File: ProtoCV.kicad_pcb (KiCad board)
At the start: 2 copper layers, 100 x 100 mm, 141 parts, among them J1 AudioJack2_SwitchT, J10 Conn_01x01_Male, J11 Conn_01x05_Male, J12 Conn_01x09_Male, J13 AudioJack2_SwitchT, J14 AudioJack2_SwitchT, J15 AudioJack2_SwitchT, J16 AudioJack2_SwitchT, J17 AudioJack2_SwitchT, J18 AudioJack2_SwitchT, J19 AudioJack2_SwitchT, J2 AudioJack2_SwitchT, J20 AudioJack2_SwitchT, J21 Conn_01x01_Male, J22 Conn_01x01_Male, J23 Conn_01x01_Male, J24 Conn_01x01_Male, J25 Conn_01x01_Male, J26 Conn_01x01_Male, J27 Conn_01x01_Male, J28 Conn_01x01_Male, J29 Conn_01x01_Male, J3 AudioJack2_SwitchT, J30 Conn_01x01_Male, J4 AudioJack2_SwitchT, J5 AudioJack2_SwitchT, J6 AudioJack2_SwitchT, J7 AudioJack2_SwitchT, J8 AudioJack2_SwitchT, J9 Conn_02x05_Odd_Even, Q1 BC847, Q2 BC847, Q3 BC847, Q4 BC847, Q5 BC847, Q6 BC847, Q7 BC847, Q8 BC847, U1 OPA4192, U2 OPA4192, U3 ADC80508Z, U4 R-78E3.3-0.5, U5 LD2981ABU33TR, U6 74AHCT244, U7 L7805

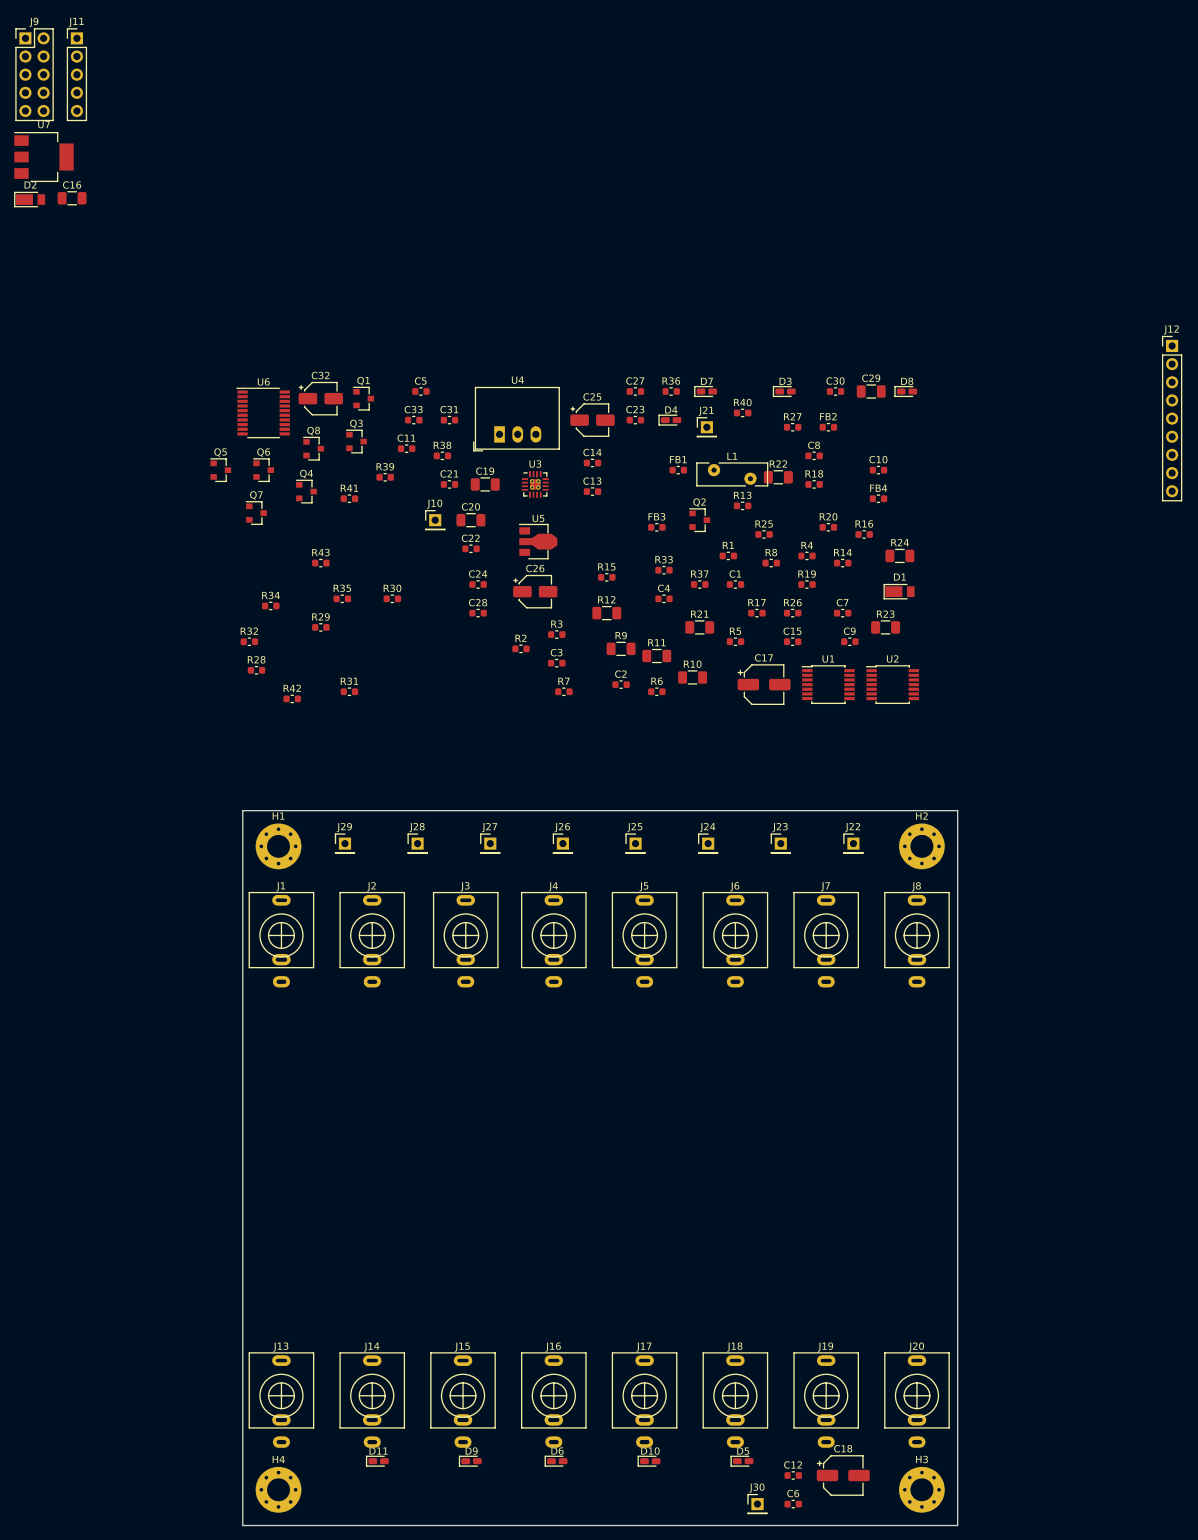
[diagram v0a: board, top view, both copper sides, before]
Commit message: Completed placement.
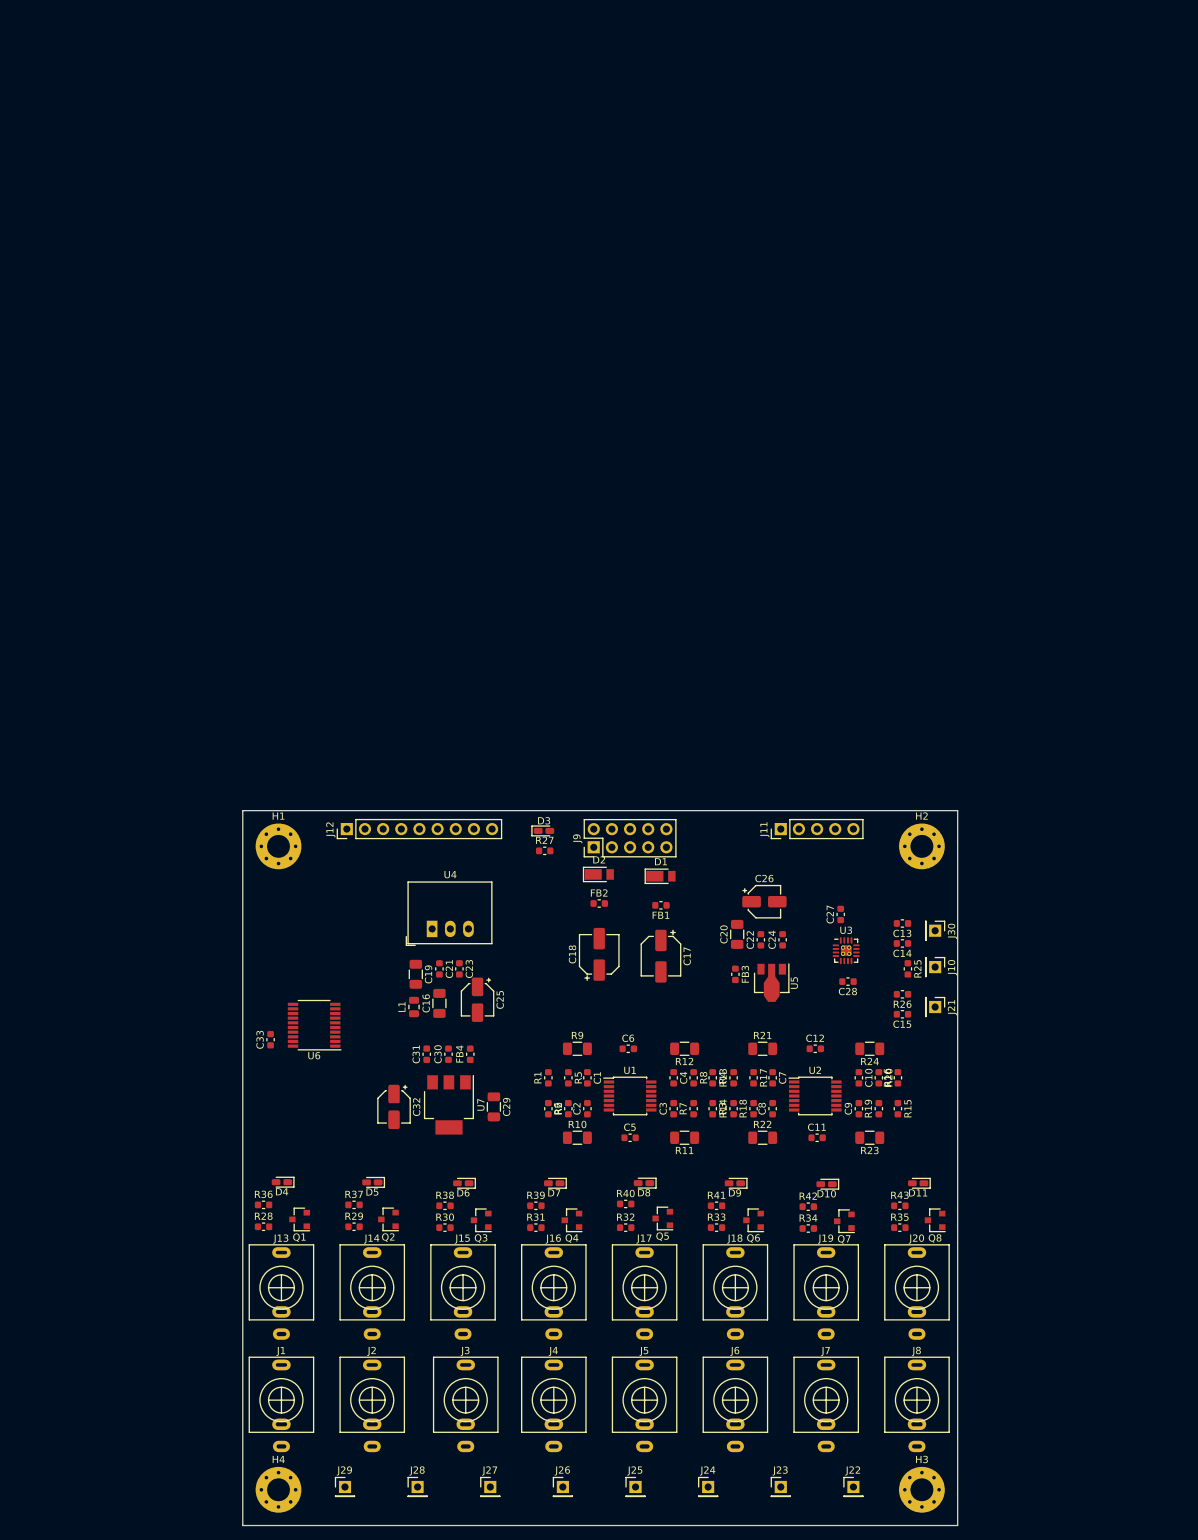
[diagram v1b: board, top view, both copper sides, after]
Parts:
- L1: footprint Fuse:Fuse_Bourns_MF-RHT100 -> Inductor_SMD:L_0805_2012Metric
- moved J11 148.1 mm to (175.3, 52.6), turned to 90 degrees
- moved U7 144.2 mm to (128.8, 91.2), turned to 270 degrees
- moved Q8 138.6 mm to (196.8, 107.3), turned to 180 degrees
- moved J9 138.3 mm to (149.1, 55.1), turned to 90 degrees
- moved J12 133.8 mm to (114.6, 52.6), turned to 90 degrees
- moved Q7 128.7 mm to (184.2, 107.4), turned to 180 degrees
- moved R36 127.3 mm to (102.9, 105.1)
- moved Q6 125.3 mm to (171.4, 107.3), turned to 180 degrees
- moved C16 123.8 mm to (127.5, 77.0), turned to 90 degrees
- moved D2 123.5 mm to (149.9, 58.9)
- moved Q5 121.6 mm to (158.8, 107.1), turned to 180 degrees
- moved R43 121.0 mm to (191.9, 105.3)
- moved D4 119.7 mm to (105.5, 102.0), turned to 180 degrees
- moved R35 117.6 mm to (191.9, 108.3)
- moved D8 116.7 mm to (156.1, 102.1), turned to 180 degrees
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
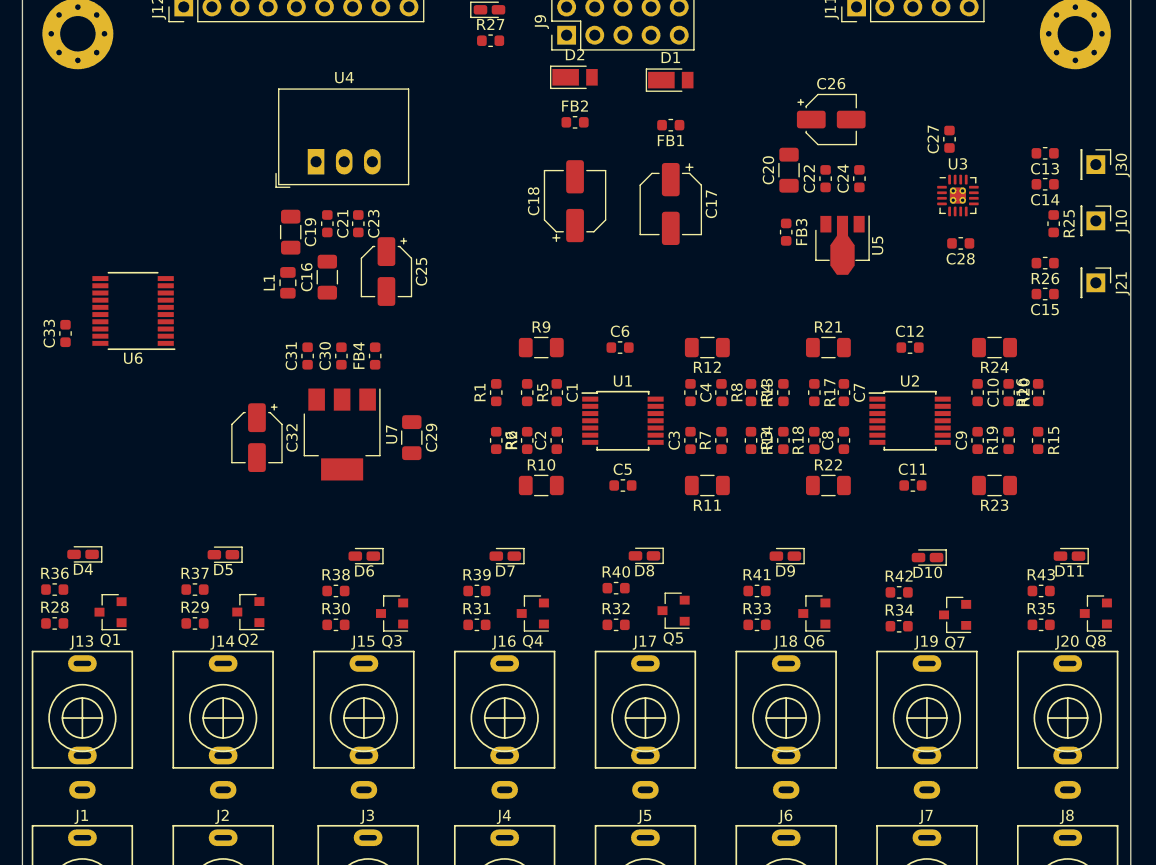
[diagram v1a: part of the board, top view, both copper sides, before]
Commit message: Improved placement with separate analogue section.
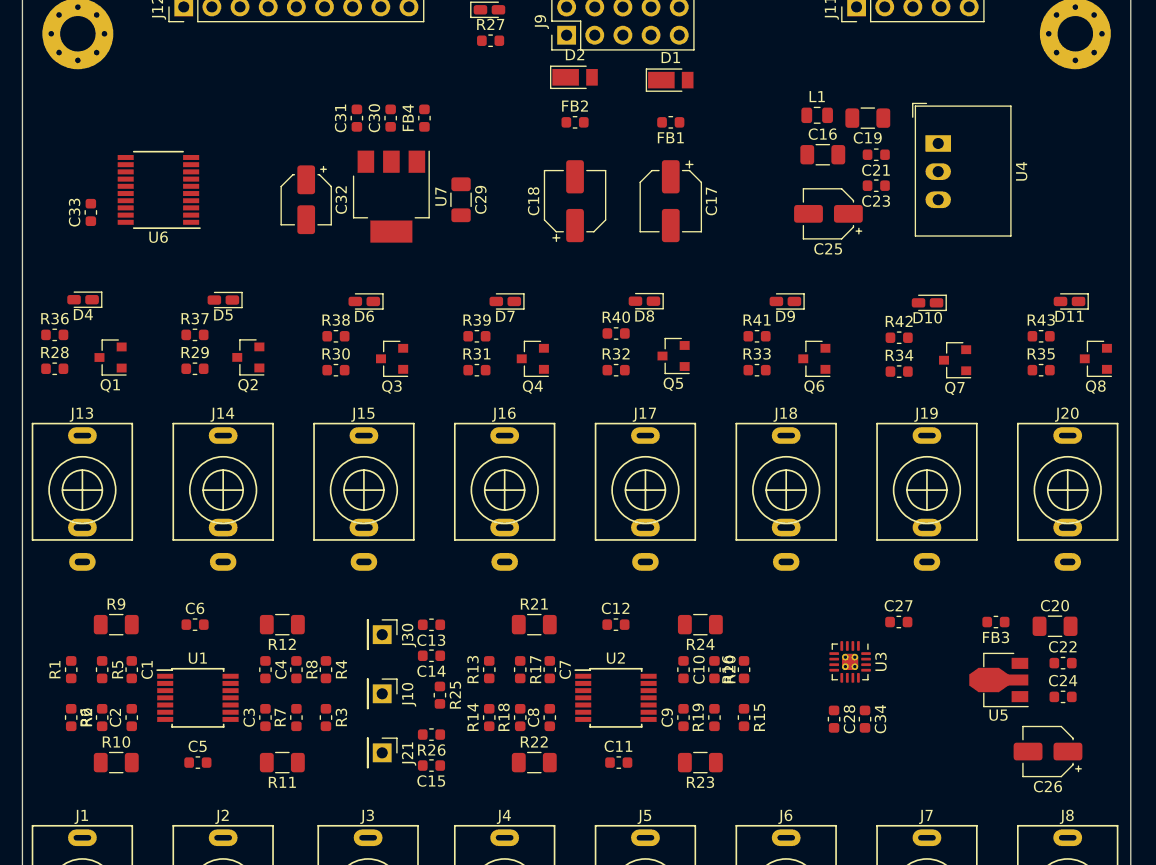
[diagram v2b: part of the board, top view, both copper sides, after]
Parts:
- added C34: 1n, Capacitor_SMD:C_0603_1608Metric, F.Cu at (176.0, 116.8)
- moved J10 77.2 mm to (132.5, 114.6)
- moved J21 77.1 mm to (132.5, 119.9)
- moved J30 77.1 mm to (132.5, 109.2)
- moved C14 69.8 mm to (136.9, 111.1)
- moved R25 69.8 mm to (137.7, 114.7)
- moved R26 69.8 mm to (136.9, 118.2)
- moved C13 69.8 mm to (136.9, 108.3)
- moved C15 69.8 mm to (136.9, 121.0)
- moved C26 60.3 mm to (192.5, 119.8), turned to 180 degrees
- moved U4 56.2 mm to (182.6, 64.9), turned to 270 degrees
- moved C19 53.1 mm to (176.3, 62.6), turned to 180 degrees
- moved C24 50.2 mm to (193.9, 114.8), turned to 0 degrees
- moved L1 50.1 mm to (171.7, 62.4), turned to 0 degrees
- moved C21 49.9 mm to (177.0, 65.9), turned to 180 degrees
- moved C22 48.7 mm to (193.9, 111.8), turned to 0 degrees
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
